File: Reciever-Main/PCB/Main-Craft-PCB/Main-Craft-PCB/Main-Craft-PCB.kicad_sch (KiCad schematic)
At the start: 126 parts, among them J1 nRF24L01_Conn, J10 L298N, J2 IR_SENSOR_?, J3 IR_SENSOR_?, J4 IR_SENSOR_?, J5 IR_SENSOR_?, J6 ESC_?, J7 ESC_?, J8 ESC_?, J9 ESC_?, Q1 2N2219, Q10 2N2219, Q11 2N2219, Q12 2N2219, Q13 2N2219, Q14 2N2219, Q2 2N2219, Q3 2N2219, Q4 2N2219, Q5 2N2219, Q6 2N2219, Q7 2N2219, Q8 2N2219, Q9 2N2219, SW1 SW_Push, SW2 SW_Push, SW3 SW_Push, SW4 SW_SPDT, SW5 SW_SPDT, SW6 SW_SPDT, SW7 SW_SPDT, SW8 SW_SPDT, U1 NUCLEO144-F429ZI, U2 LM741, U3 LM741, U4 LM2940-3.0, U5 LM2940-5.0, U6 LM2940-12.0

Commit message: Update PCB and start pon layout
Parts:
- removed F1: Fuse, symbol Device:Fuse
- removed R20, R23, R29: 1K, Resistor_SMD:R_0603_1608Metric, symbol Device:R
- removed R22, R24, R26: 10K, Resistor_SMD:R_0603_1608Metric, symbol Device:R
- removed SW3: SW_Push, symbol Switch:SW_Push
- removed SW4: SW_SPDT, My_library:KNX-1-D1, symbol Switch:SW_SPDT
- D17: footprint My_library:1N5817M -> Diode_SMD:D_0603_1608Metric
- J1: footprint (none) -> Connector_PinHeader_2.54mm:PinHeader_2x04_P2.54mm_Vertical_SMD
- J10: footprint (none) -> Connector_PinHeader_2.54mm:PinHeader_1x06_P2.54mm_Vertical_SMD_Pin1Left
- J2: value IR_SENSOR_? -> IR_SENSOR_1; footprint (none) -> Connector_PinHeader_2.54mm:PinHeader_1x03_P2.54mm_Vertical_SMD_Pin1Left
- J3: value IR_SENSOR_? -> IR_SENSOR_2; footprint (none) -> Connector_PinHeader_2.54mm:PinHeader_1x03_P2.54mm_Vertical_SMD_Pin1Left
- J4, J5: footprint (none) -> Connector_PinHeader_2.54mm:PinHeader_1x03_P2.54mm_Vertical_SMD_Pin1Left
- J6: value ESC_? -> ESC_1; footprint (none) -> Connector_PinHeader_2.54mm:PinHeader_1x03_P2.54mm_Vertical_SMD_Pin1Left
- J7: value ESC_? -> ESC_2; footprint (none) -> Connector_PinHeader_2.54mm:PinHeader_1x03_P2.54mm_Vertical_SMD_Pin1Left
- J8: value ESC_? -> ESC_3; footprint (none) -> Connector_PinHeader_2.54mm:PinHeader_1x03_P2.54mm_Vertical_SMD_Pin1Left
- J9: value ESC_? -> ESC_4; footprint (none) -> Connector_PinHeader_2.54mm:PinHeader_1x03_P2.54mm_Vertical_SMD_Pin1Left
- Q1, Q10, Q11, Q12, Q13, Q14, Q2, Q3, Q4, Q5, Q6, Q7, Q8, Q9: footprint Package_TO_SOT_THT:TO-39-3 -> Package_TO_SOT_SMD:SOT-23
- SW1, SW2: footprint (none) -> Button_Switch_SMD:SW_Push_1P1T_NO_6x6mm_H9.5mm
- SW5, SW6, SW7, SW8: footprint My_library:KNX-1-D1 -> My_library:JS202011SCQN
- U1: footprint Module:ST_Morpho_Connector_144_STLink -> My_library:MODULE_NUCLEO-F429ZI
- U6: footprint My_library:KNX-1-D1 -> Package_TO_SOT_SMD:SOT-223
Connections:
- net NRF_CE is gone; now on net CE: J1.3 (Pin_3)
- net NRF_CSN is gone; now on net CSN: J1.4 (Pin_4)
- net NRF_IRQ is gone; now on net IRQ: J1.8 (Pin_8)
- net NRF_MOSI is gone; now on net MOSI: J1.6 (Pin_6)
- net NRF_SCK is gone; now on net SCK: J1.5 (Pin_5)
- net MOSI: no longer U1.99 (PB4)
- net MOTOR_2_A: now also U1.47 (PE3); no longer U1.46 (PE2)
- net SW_4: now also R31.2; no longer R27.2
- net SW_5: now also R27.2, R38.2; no longer R34.2
- net SW_6: now also R34.2; no longer R38.2
- net at SW8.2 (B): now also BT1.1 (+)
- net NRF_MISO renamed MISO
- net MISO: now also U1.99 (PB4)
- net SW_7: no longer names the net of U1.125 (PE15)
- net SW_7: no longer R31.2
- net SW_8: no longer names the net of U1.97 (PB10)
- net SW_9: no longer names the net of U1.90 (PB11)
- no-connect marks 89 -> 91
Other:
- moved on the sheet: R31, R33, R35, R38, SW6

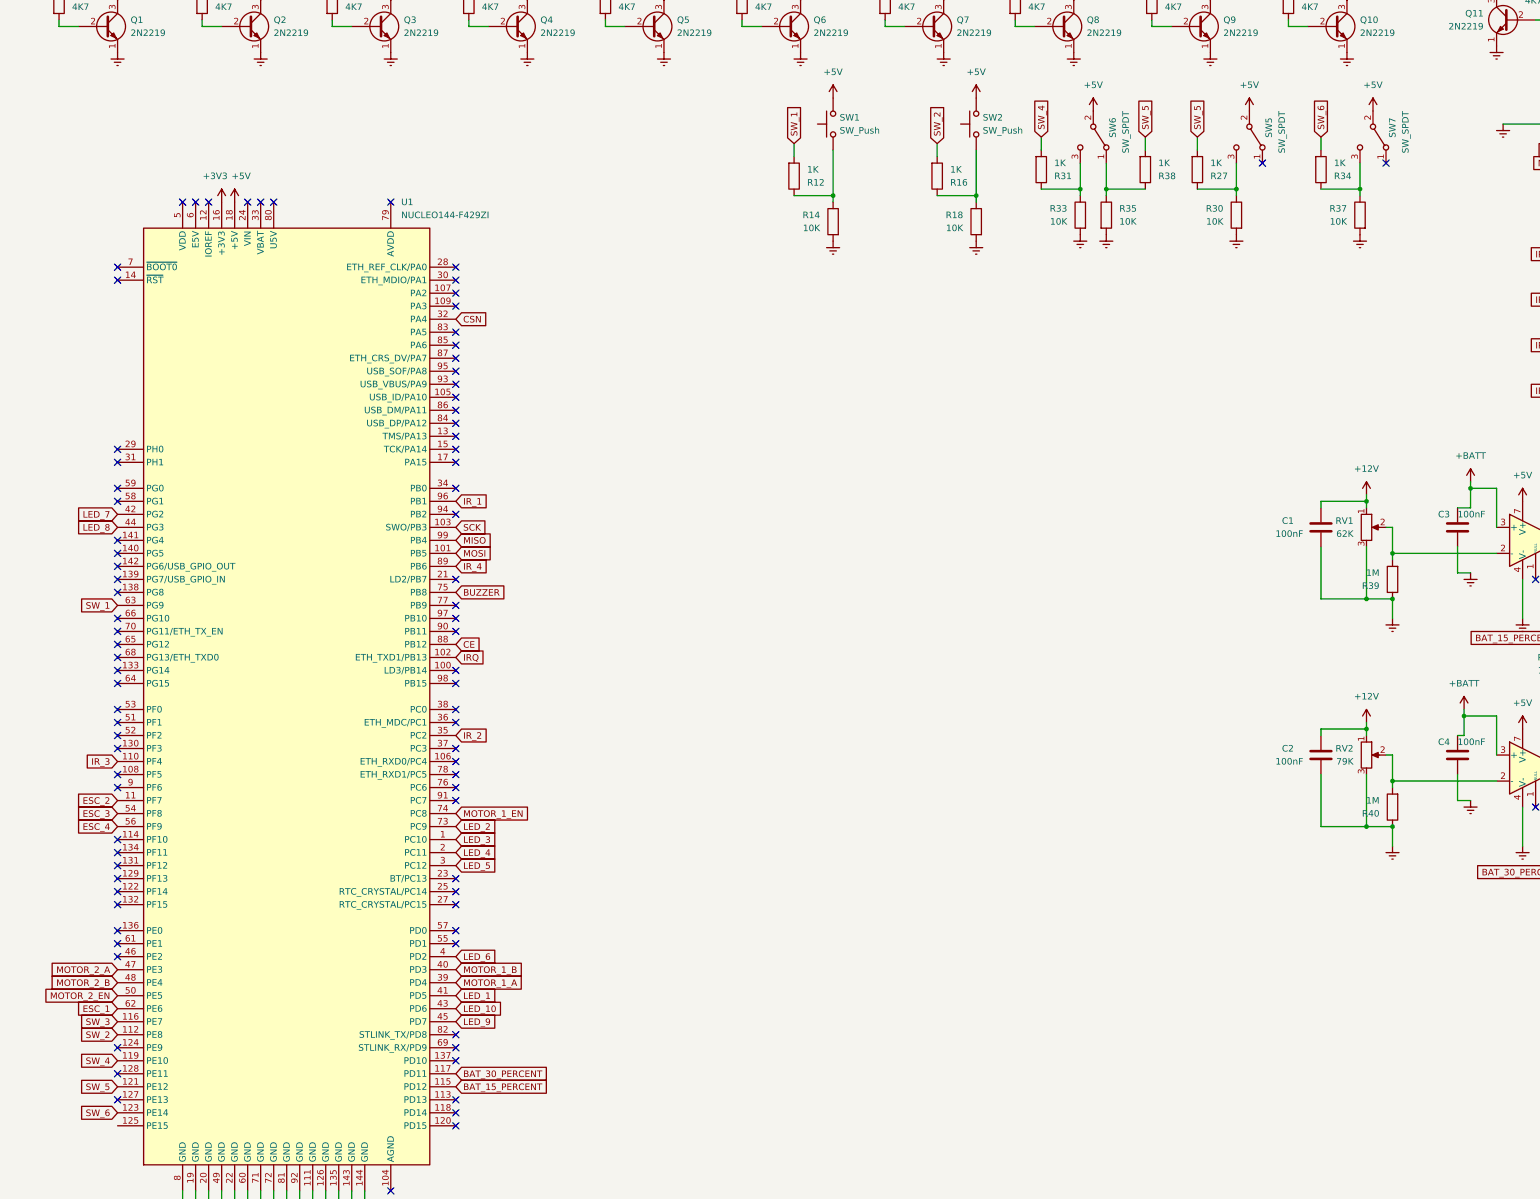
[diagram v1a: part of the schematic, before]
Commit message: Start Routing for tracks on PCB
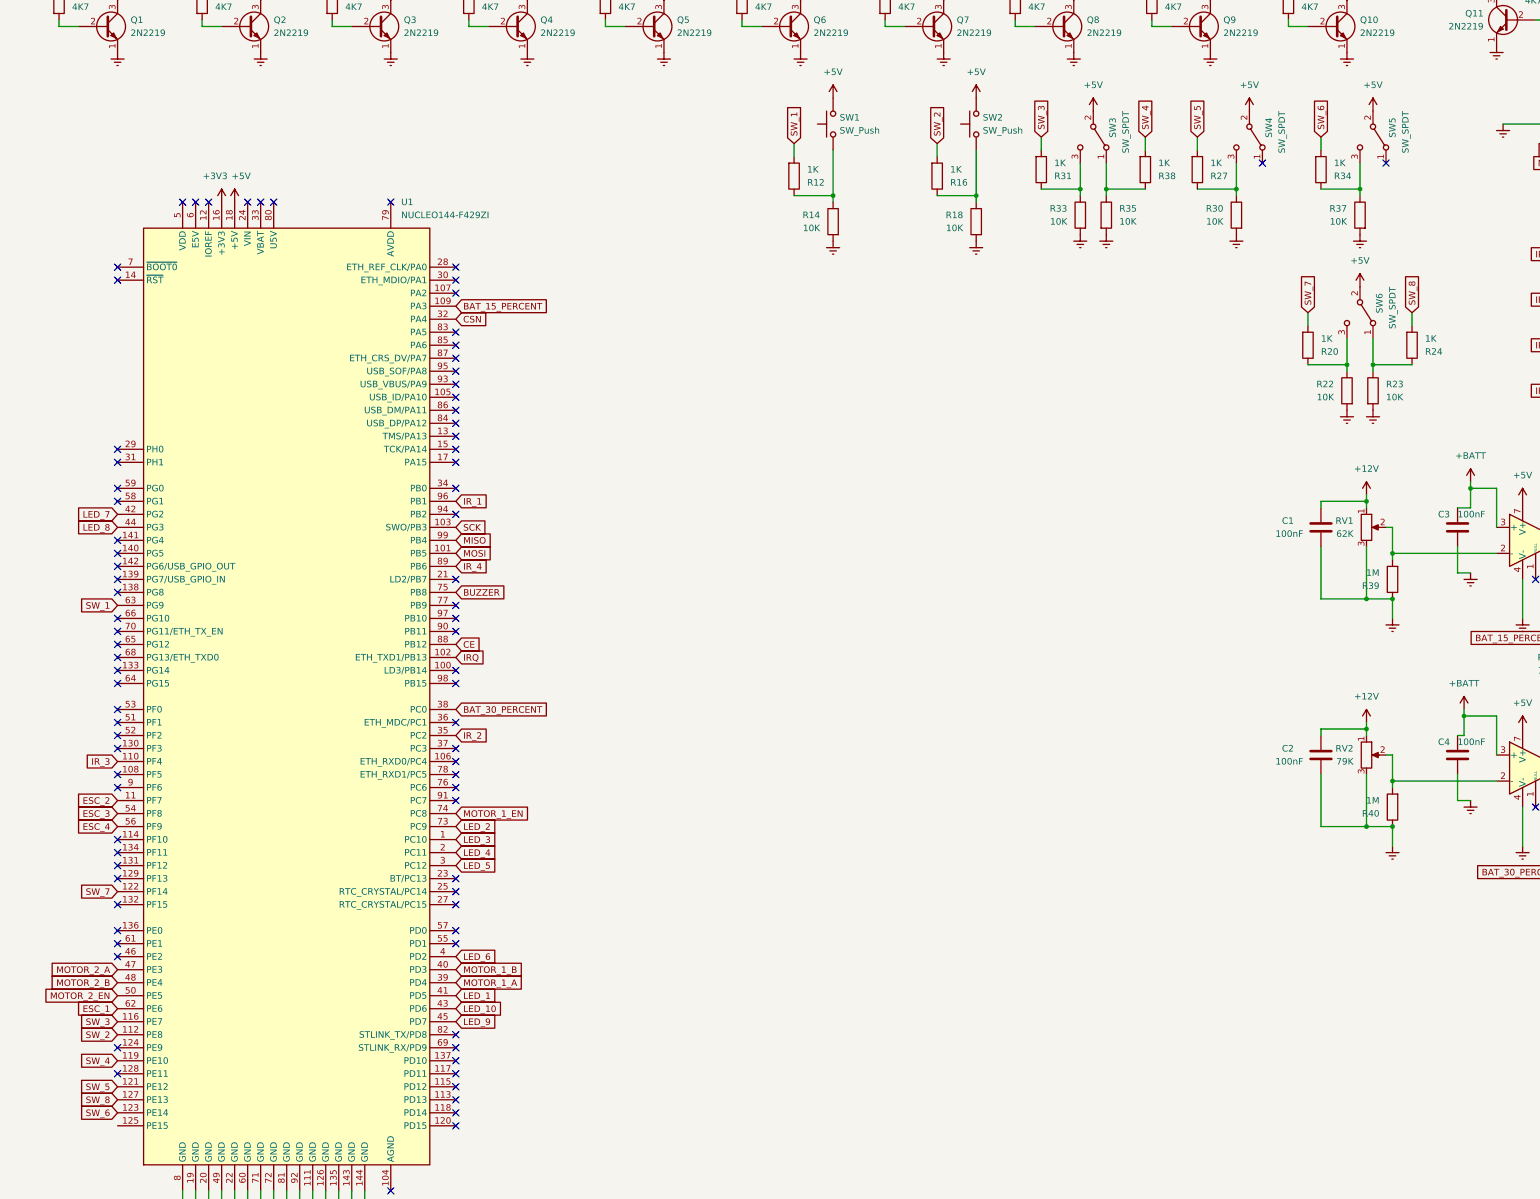
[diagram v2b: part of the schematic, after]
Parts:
- added R20, R24: 1K, Resistor_SMD:R_0603_1608Metric, symbol Device:R
- added R22, R23: 10K, Resistor_SMD:R_0603_1608Metric, symbol Device:R
- added SW6: SW_SPDT, My_library:JS202011SCQN, symbol Switch:SW_SPDT
- J10: footprint Connector_PinHeader_2.54mm:PinHeader_1x06_P2.54mm_Vertical_SMD_Pin1Left -> Connector_PinHeader_2.54mm:PinHeader_1x06_P2.54mm_Vertical
- J2, J3, J4, J5, J6, J7, J8, J9: footprint Connector_PinHeader_2.54mm:PinHeader_1x03_P2.54mm_Vertical_SMD_Pin1Left -> Connector_PinHeader_2.54mm:PinHeader_1x03_P2.54mm_Vertical
- SW8: footprint My_library:JS202011SCQN -> My_library:KNX-1-D1
- U1: footprint My_library:MODULE_NUCLEO-F429ZI -> My_library:MODULE_NUCLEO-F429ZI_JUST_PINS
- renumbered SW6 to SW3, SW5 to SW4, SW7 to SW5
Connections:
- net +5V: now also SW6.2 (B)
- net BAT_15_PERCENT: now also U1.109 (PA3); no longer U1.115 (PD12)
- net BAT_30_PERCENT: now also U1.38 (PC0); no longer U1.117 (PD11)
- net Earth: now also R22.2, R23.2
- net SW_3: now also R31.2
- net SW_4: now also R38.2; no longer R31.2
- net SW_5: no longer R38.2
- net SW_7: now reaches U1.122 (PF14)
- net SW_7: now also R20.2
- net SW_8: now reaches U1.127 (PE13)
- net SW_8: now also R24.2
- new net: R20.1, R22.1, SW6.3 (C)
- new net: R23.1, R24.1, SW6.1 (A)
- no-connect marks 91 -> 89

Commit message: Add Gerber files CPL files and update footprints for componetns
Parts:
- removed U2, U3: LM741, My_library:741C, symbol Amplifier_Operational:LM741
- added R35, R36: 47K, Resistor_SMD:R_0603_1608Metric, symbol Device:R
- added U2: LM358DR2G, symbol Amplifier_Operational:LM358
- BT1: footprint (none) -> Connector_PinHeader_2.54mm:PinHeader_1x02_P2.54mm_Vertical
- D1, D10, D17, D2, D3, D4, D5, D6, D7, D8, D9: value LED -> BLUE
- D11, D12, D19: value LED -> GREEN
- D13, D18: value LED -> YELLOW
- D14, D15, D16: footprint My_library:1N5817M -> My_library:SOD-123
- R10, R13, R17, R2, R21, R4, R41, R49, R50, R6, R8: value 10K -> 1K
- R27: renamed from R28; value 10K -> 1K
- R32: renamed from R36; value 10K -> 1K
- RV1: value 62K -> 15K; footprint My_library:35WR100KLFTR -> My_library:Variable_Resistor
- RV2: value 79K -> 32K; footprint My_library:35WR100KLFTR -> My_library:Variable_Resistor
- renumbered R31 to R20, R33 to R22, R35 to R23, R38 to R24, R27 to R26, R30 to R28, R32 to R29, R20 to R30, R34 to R31, R22 to R33, R37 to R34, R23 to R37, R39 to R38, R40 to R39, R24 to R40, SW6 to SW5, SW5 to SW6, SW8 to SW7, U4 to U3, U5 to U4, U6 to U5
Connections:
- net +12V: now also R35.2, R36.2; no longer RV1.1, RV2.1
- net +5V: now also U2.8 (V+)
- net +BATT: now also U2.3 (+), U2.5 (+)
- net Earth: now also U2.4 (V-)
- net SW_2: now also U1.116 (PE7); no longer U1.112 (PE8)
- net SW_3: now also U1.112 (PE8); no longer U1.116 (PE7)
- net at R44.1: now also U2.1
- net at R38.2, RV1.2: now also U2.2 (-)
- net at R45.1: now also U2.7
- net at R39.2, RV2.2: now also U2.6 (-)
- new net: R35.1, RV1.1
- new net: R36.1, RV2.1
- no-connect marks 89 -> 85
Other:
- moved on the sheet: BT1, RV1, RV2
